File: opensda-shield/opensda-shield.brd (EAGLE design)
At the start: 21.6 x 53.3 mm, 17 parts, among them IC1 74LVC125, IC2 74LVC125, J1 61302011121, J2 61302011121, J3 61300211121, J4 CORTEX_DEBUG_PTH, J5 61301511121

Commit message: Zmeny z e-mailu
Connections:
- net N$1 renamed 3V3_OUT
- net N$3 renamed USB5V_OUT
- net PTA4 renamed !SDA_SWD_EN_PTA4
- net PTB0 renamed !SDA_SWD_OE_PTB0
- net PTB1 renamed !SDA_RST_TGTMCU_PTB1
- net PTC3 renamed UART0_TX_TGTMCU_PTC3
- net PTC4 renamed UART0_RX_TGTMCU_PTC4
- net PTC5 renamed SDA_SPI0_SCK_PTC5
- net PTC6 renamed SDA_SPI0_SOUT_PTC6
- net PTC7 renamed SDA_SPI0_SIN_PTC7
- net PTD4 renamed !SDA_LED_PTD4
- net RST_TGT renamed !RST_TGT
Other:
- board text removed: "PTB1"
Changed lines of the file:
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@@
 <layer number="23" name="tOrigins" color="15" fill="1" visible="yes" active="yes"/>
 <layer number="24" name="bOrigins" color="15" fill="1" visible="yes" active="yes"/>
-<layer number="25" name="tNames" color="7" fill="1" visible="yes" active="yes"/>
-<layer number="26" name="bNames" color="7" fill="1" visible="yes" active="yes"/>
+<layer number="25" name="tNames" color="7" fill="1" visible="no" active="yes"/>
+<layer number="26" name="bNames" color="7" fill="1" visible="no" active="yes"/>
 <layer number="27" name="tValues" color="7" fill="1" visible="no" active="yes"/>
 <layer number="28" name="bValues" color="7" fill="1" visible="no" active="yes"/>
@@
 <text x="13.97" y="15.24" size="1.016" layer="111" ratio="15" align="center-right">TX</text>
 <text x="7.3025" y="51.1175" size="1.016" layer="111" ratio="15" rot="R180" align="top-center">PTD4</text>
-<text x="9.525" y="2.54" size="1.016" layer="111" ratio="15" rot="R180" align="center-right">PTB1</text>
 <circle x="10.795" y="37.7825" radius="0.254" width="0.1524" layer="111"/>
 <circle x="10.795" y="22.86" radius="0.254" width="0.1524" layer="111"/>
@@
 <contactref element="C2" pad="1"/>
 <wire x1="1.905" y1="43.18" x2="5.08" y2="43.18" width="0.3048" layer="1"/>
-<wire x1="9.60755" y1="17.03995" x2="9.57" y2="17.0775" width="0.3048" layer="1"/>
 <wire x1="5.08" y1="43.18" x2="6.35" y2="44.45" width="0.1524" layer="1"/>
 <wire x1="6.35" y1="47.845" x2="6.0325" y2="48.1625" width="0.1524" layer="1"/>
@@
 <contactref element="J1" pad="15"/>
 </signal>
-<signal name="PTA4">
+<signal name="!SDA_SWD_EN_PTA4">
 <contactref element="J1" pad="16"/>
 <contactref element="R2" pad="2"/>
@@
 <contactref element="J1" pad="18"/>
 </signal>
-<signal name="PTB0">
+<signal name="!SDA_SWD_OE_PTB0">
 <contactref element="J1" pad="19"/>
 <contactref element="R3" pad="2"/>
 <contactref element="IC1" pad="4"/>
-<wire x1="7.62" y1="37.85" x2="7.62" y2="35.56" width="0.1524" layer="1"/>
-<wire x1="7.62" y1="35.56" x2="7.619996875" y2="35.559996875" width="0.1524" layer="1"/>
 <via x="6.0325" y="35.56" extent="1-16" drill="0.35"/>
-<wire x1="7.62" y1="35.56" x2="6.0325" y2="35.56" width="0.1524" layer="16"/>
-<via x="7.62" y="35.56" extent="1-16" drill="0.35"/>
+<wire x1="6.0325" y1="35.56" x2="7.62" y2="35.56" width="0.1524" layer="16"/>
 <wire x1="4.1275" y1="33.3375" x2="6.0325" y2="35.56" width="0.1524" layer="1"/>
 <wire x1="5.87375" y1="9.04875" x2="1.905" y2="5.08" width="0.1524" layer="1"/>
@@
 <wire x1="5.87375" y1="15.39875" x2="5.715" y2="15.5575" width="0.1524" layer="1"/>
 <wire x1="5.715" y1="15.5575" x2="4.7625" y2="15.5575" width="0.1524" layer="1"/>
-</signal>
-<signal name="PTB1">
+<via x="7.62" y="35.56" extent="1-16" drill="0.35"/>
+<wire x1="7.62" y1="35.56" x2="7.62" y2="37.85" width="0.1524" layer="1"/>
+</signal>
+<signal name="!SDA_RST_TGTMCU_PTB1">
 <contactref element="J1" pad="20"/>
 <contactref element="R1" pad="2"/>
@@
 <contactref element="J2" pad="7"/>
 </signal>
-<signal name="PTC3">
+<signal name="UART0_TX_TGTMCU_PTC3">
 <contactref element="J2" pad="8"/>
 <contactref element="IC2" pad="6"/>
@@
 <wire x1="6.6675" y1="20.955" x2="6.6675" y2="21.9075" width="0.1524" layer="16"/>
 </signal>
-<signal name="PTC4">
+<signal name="UART0_RX_TGTMCU_PTC4">
 <contactref element="J2" pad="9"/>
 <contactref element="IC2" pad="2"/>
@@
 <wire x1="9.54405" y1="24.14905" x2="16.49095" y2="24.14905" width="0.1524" layer="1"/>
 </signal>
-<signal name="PTC5">
+<signal name="SDA_SPI0_SCK_PTC5">
 <contactref element="J2" pad="10"/>
 <wire x1="18.44675" y1="26.63825" x2="19.685" y2="25.4" width="0.1524" layer="1"/>
@@
 <wire x1="8.27" y1="31.1889" x2="12.82065" y2="26.63825" width="0.1524" layer="1"/>
 </signal>
-<signal name="PTC6">
+<signal name="SDA_SPI0_SOUT_PTC6">
 <contactref element="J2" pad="11"/>
 <contactref element="IC1" pad="5"/>
@@
 <wire x1="15.875" y1="31.75" x2="13.0175" y2="31.75" width="0.1524" layer="1"/>
 </signal>
-<signal name="PTC7">
+<signal name="SDA_SPI0_SIN_PTC7">
 <contactref element="J2" pad="12"/>
 <contactref element="IC1" pad="3"/>
@@
 <contactref element="J2" pad="16"/>
 </signal>
-<signal name="PTD4">
+<signal name="!SDA_LED_PTD4">
 <contactref element="J2" pad="17"/>
 <contactref element="R5" pad="2"/>
@@
 <wire x1="15.23365" y1="25.39365" x2="13.4493" y2="25.39365" width="0.1524" layer="1"/>
 <wire x1="7.62" y1="31.22295" x2="13.4493" y2="25.39365" width="0.1524" layer="1"/>
-<wire x1="17.4498" y1="21.971" x2="17.4498" y2="21.9202" width="0.1524" layer="1"/>
 <wire x1="17.4498" y1="21.9202" x2="17.4498" y2="14.5542" width="0.1524" layer="1"/>
 <wire x1="11.7475" y1="8.255" x2="11.7475" y2="8.8519" width="0.1524" layer="1"/>
@@
 <wire x1="17.145" y1="22.225" x2="17.4498" y2="21.9202" width="0.1524" layer="1"/>
 </signal>
-<signal name="RST_TGT">
+<signal name="!RST_TGT">
 <contactref element="J5" pad="10"/>
 <contactref element="J4" pad="10"/>
@@
 <contactref element="IC2" pad="12"/>
 <wire x1="6.32" y1="17.0775" x2="6.97" y2="17.0775" width="0.1524" layer="1"/>
-<wire x1="9.2075" y1="14.6025" x2="9.17195" y2="14.6025" width="0.1524" layer="1"/>
-<wire x1="9.2075" y1="14.73205" x2="9.2075" y2="14.6025" width="0.1524" layer="1"/>
+<wire x1="9.2075" y1="14.73205" x2="9.2075" y2="14.605" width="0.1524" layer="1"/>
 <wire x1="8.255" y1="16.1925" x2="8.89" y2="16.1925" width="0.1524" layer="1"/>
-<wire x1="8.89" y1="16.1925" x2="8.92" y2="16.1925" width="0.1524" layer="1"/>
 <wire x1="8.92" y1="17.0775" x2="8.92" y2="16.2225" width="0.1524" layer="1"/>
 <wire x1="8.92" y1="16.2225" x2="8.89" y2="16.1925" width="0.1524" layer="1"/>
@@
 <wire x1="7.3025" y1="16.1925" x2="8.255" y2="16.1925" width="0.1524" layer="1"/>
 <wire x1="9.2075" y1="15.875" x2="8.89" y2="16.1925" width="0.1524" layer="1"/>
-<wire x1="9.2075" y1="14.6025" x2="9.2075" y2="15.875" width="0.1524" layer="1"/>
-</signal>
-<signal name="N$1">
+<wire x1="9.2075" y1="14.73205" x2="9.2075" y2="15.875" width="0.1524" layer="1"/>
+<wire x1="9.2075" y1="14.6025" x2="9.2075" y2="14.605" width="0.1524" layer="1"/>
+</signal>
+<signal name="3V3_OUT">
 <contactref element="J5" pad="3"/>
 <contactref element="JP1" pad="3"/>
 <wire x1="7.62" y1="45.72" x2="15.24" y2="45.72" width="0.3048" layer="1"/>
 </signal>
-<signal name="N$3">
+<signal name="USB5V_OUT">
 <contactref element="J5" pad="4"/>
 <contactref element="JP1" pad="1"/>

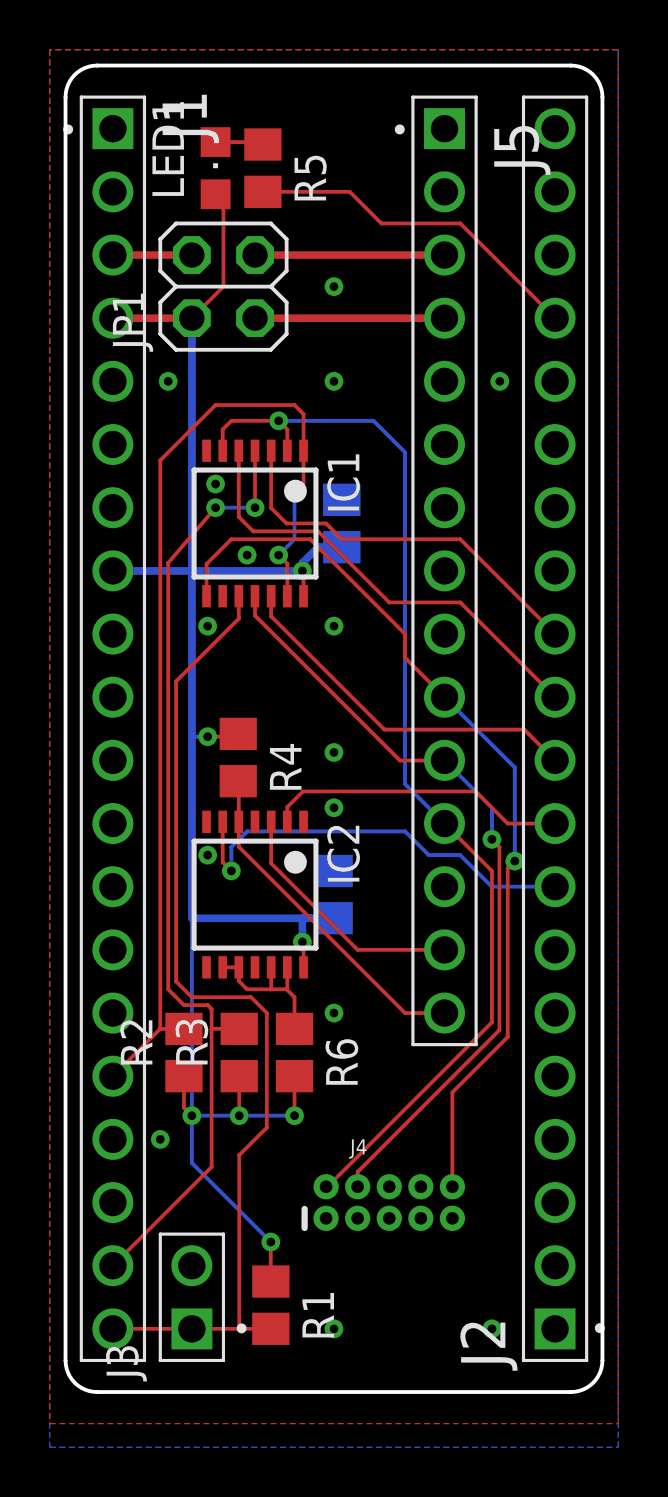
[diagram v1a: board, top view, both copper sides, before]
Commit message: presun odporu
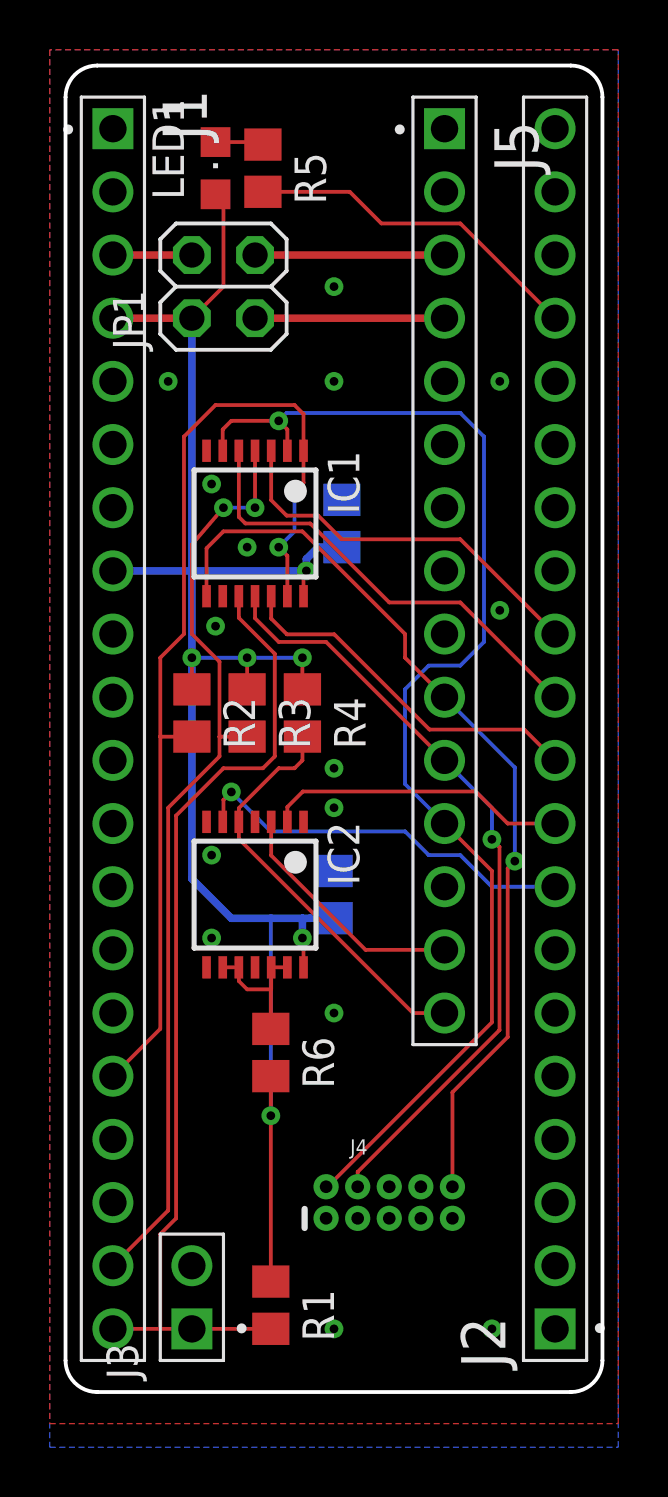
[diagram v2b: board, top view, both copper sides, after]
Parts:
- moved R2 13.7 mm to (5.08, 27.3), turned to 270 degrees
- moved R3 13.7 mm to (7.30, 27.3), turned to 270 degrees
- moved R4 3.14 mm to (9.53, 27.3)
- moved R6 0.95 mm to (8.26, 13.7)
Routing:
- net SWD_DIO_TGT: track 44.0 -> 49.8 mm
- net 3V3: track 78.3 -> 75.1 mm, vias 7 -> 6
- net TX_TGT: track 13.7 -> 16.7 mm
- net UART0_TX_TGTMCU_PTC3: track 17.3 -> 15.9 mm
- net !SDA_SWD_OE_PTB0: track 39.1 -> 37.9 mm
- net N$5: track 6.77 -> 5.76 mm
- net !SDA_RST_TGTMCU_PTB1: track 40.2 -> 39.2 mm
- net !RST_TGT: track 36.4 -> 37.0 mm

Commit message: Zmeny popisku
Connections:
- net 3V3_OUT: now also J5.4, JP1.1; no longer J5.3, JP1.3
- net USB5V_OUT: now also J5.3, JP1.3; no longer J5.4, JP1.1
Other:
- board text added: "BOOT"
- board text added: "SDA_LED"
- board text removed: "BSEL"
- board text removed: "PTD4"
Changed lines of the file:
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@@
 <text x="13.97" y="17.78" size="1.016" layer="111" ratio="15" align="center-right">RX</text>
 <text x="13.97" y="15.24" size="1.016" layer="111" ratio="15" align="center-right">TX</text>
-<text x="7.3025" y="51.1175" size="1.016" layer="111" ratio="15" rot="R180" align="top-center">PTD4</text>
+<text x="7.3025" y="51.435" size="1.016" layer="111" ratio="15" rot="R180" align="top-center">SDA_LED</text>
 <circle x="10.4775" y="37.7825" radius="0.254" width="0.1524" layer="111"/>
 <circle x="10.4775" y="22.86" radius="0.254" width="0.1524" layer="111"/>
@@
 <circle x="13.97" y="51.7525" radius="0.0762" width="0.3048" layer="111"/>
 <circle x="18.415" y="1.5875" radius="0.0762" width="0.3048" layer="111"/>
-<text x="4.1275" y="7.62" size="1.016" layer="111" ratio="15" align="center-left">BSEL</text>
+<text x="5.715" y="6.985" size="1.016" layer="111" ratio="15" align="bottom-center">BOOT</text>
 <text x="8.89" y="6.35" size="1.016" layer="111">1</text>
 </plain>
@@
 </signal>
 <signal name="3V3_OUT">
+<contactref element="J5" pad="4"/>
+<contactref element="JP1" pad="1"/>
+<wire x1="7.62" y1="43.18" x2="15.24" y2="43.18" width="0.3048" layer="1"/>
+</signal>
+<signal name="USB5V_OUT">
 <contactref element="J5" pad="3"/>
 <contactref element="JP1" pad="3"/>
 <wire x1="7.62" y1="45.72" x2="15.24" y2="45.72" width="0.3048" layer="1"/>
 </signal>
-<signal name="USB5V_OUT">
-<contactref element="J5" pad="4"/>
-<contactref element="JP1" pad="1"/>
-<wire x1="7.62" y1="43.18" x2="15.24" y2="43.18" width="0.3048" layer="1"/>
-</signal>
 </signals>

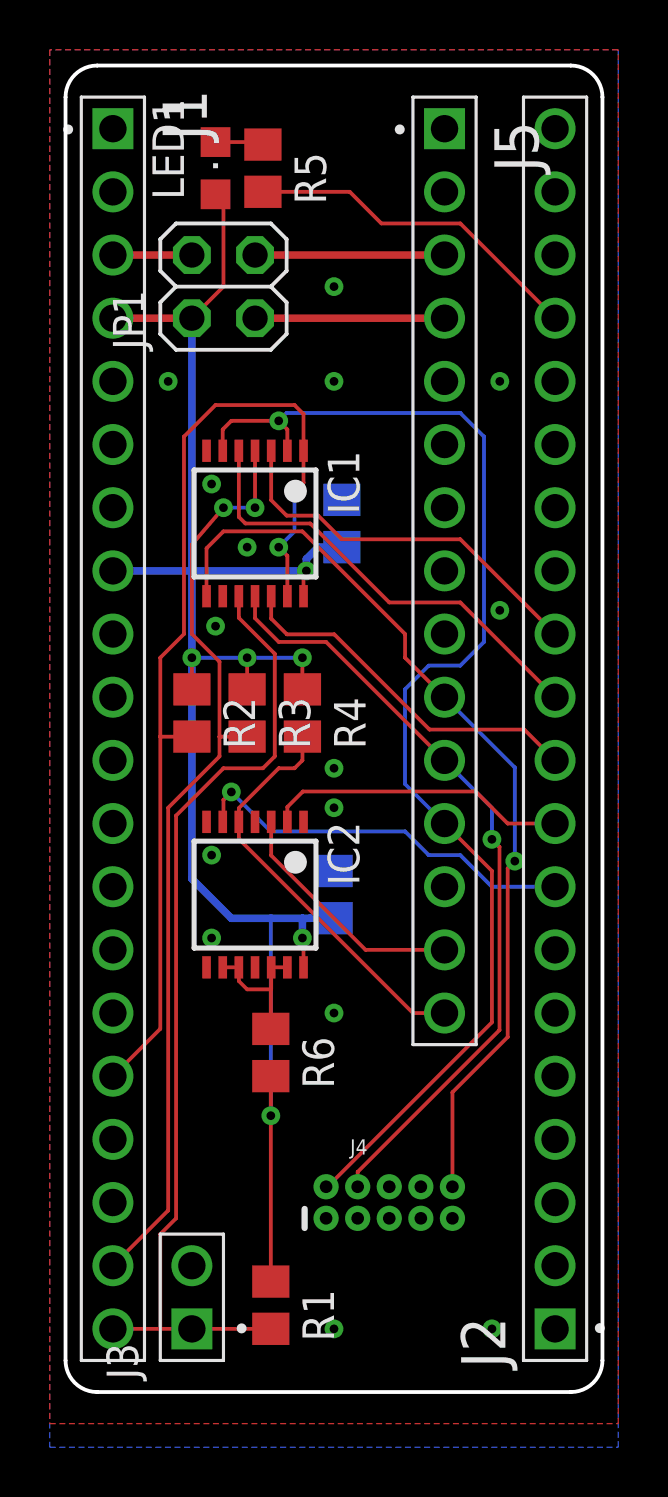
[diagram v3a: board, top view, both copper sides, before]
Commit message: Posunuti 10pin konektoru a zmena 2x2 jumperu na 3x2
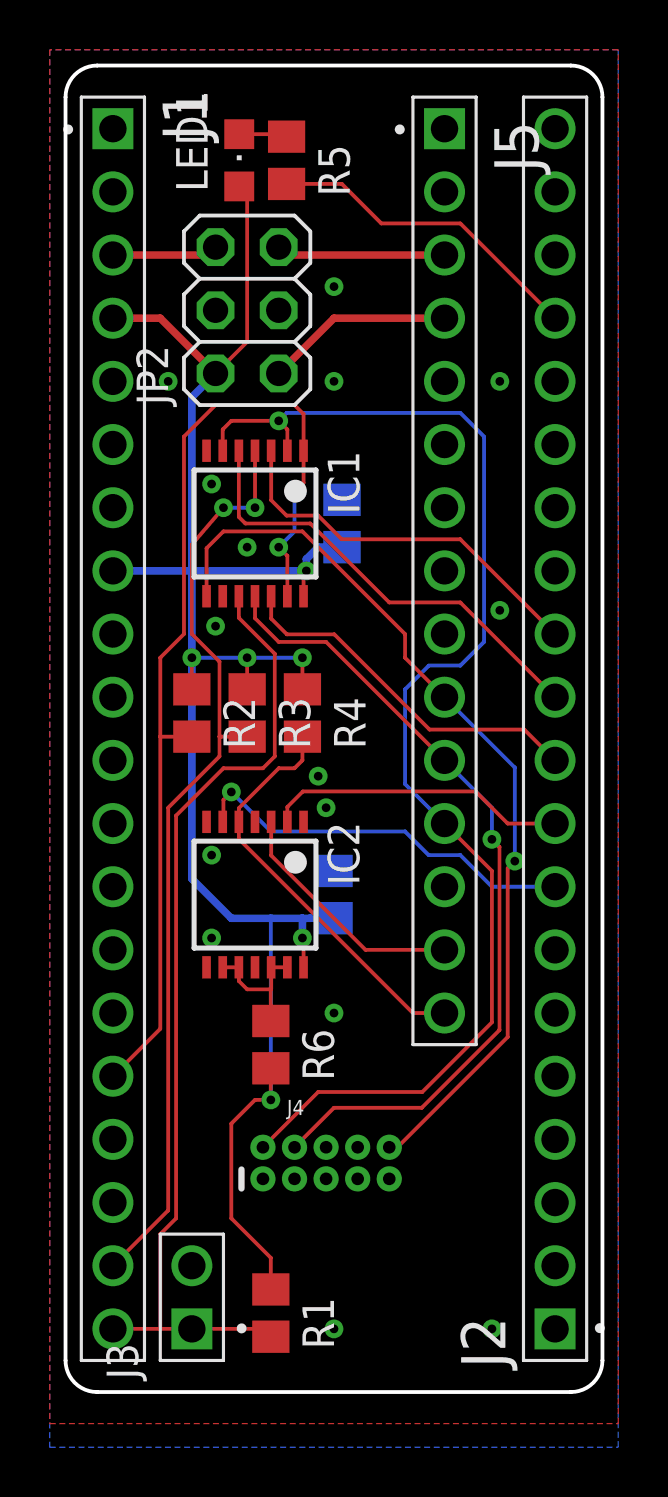
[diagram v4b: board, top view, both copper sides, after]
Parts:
- removed JP1: (no value), pinhead:2X02
- added JP2: (no value), pinhead:2X03
- moved J4 3.00 mm to (10.5, 9.21)
- moved LED1 1.00 mm to (6.99, 49.5)
- moved R5 1.00 mm to (8.89, 49.5)
- moved R6 0.32 mm to (8.26, 14.0)
- moved R1 0.32 mm to (8.26, 3.17)
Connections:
- net 3V3: now also JP2.2; no longer JP1.2
- net 3V3_OUT: now also JP2.1; no longer JP1.1
- net USB5V: now also JP2.6; no longer JP1.4
- net USB5V_OUT: now also JP2.5; no longer JP1.3
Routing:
- net 3V3: track 75.1 -> 79.4 mm
- net SWD_DIO_TGT: track 49.8 -> 51.7 mm
- net SWD_CLK_TGT: track 31.3 -> 32.8 mm
- net USB5V: track 3.17 -> 4.26 mm
- net !SDA_LED_PTD4: track 13.9 -> 13.0 mm
- net USB5V_OUT: track 7.62 -> 6.80 mm
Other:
- board text added: "OpenSDA shield"
